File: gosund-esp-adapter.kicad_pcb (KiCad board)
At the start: 2 copper layers, 18.7 x 20.3 mm, 10 parts, among them J1 Connector, J2 Conn_01x04_Male, J3 Conn_01x01_Male, U1 ESP-M2

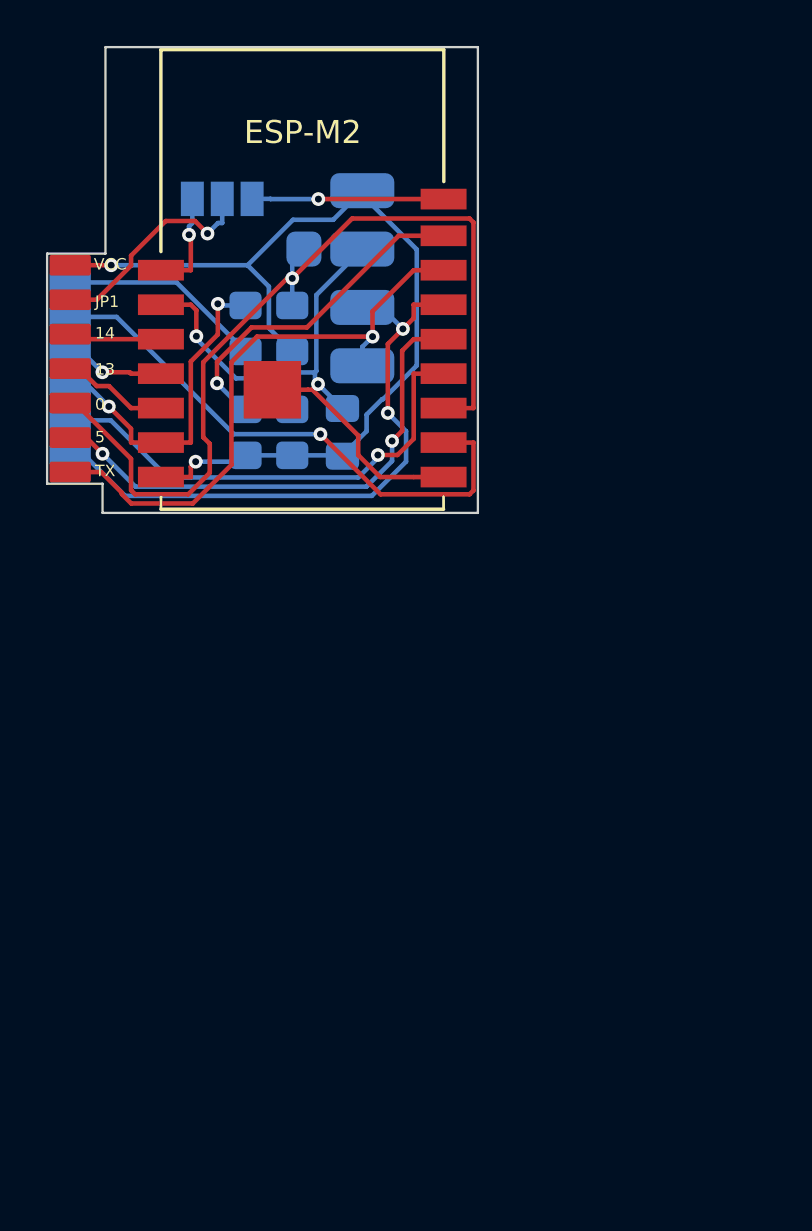
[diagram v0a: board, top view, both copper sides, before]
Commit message: modified to match the footprint of an ESP12f module
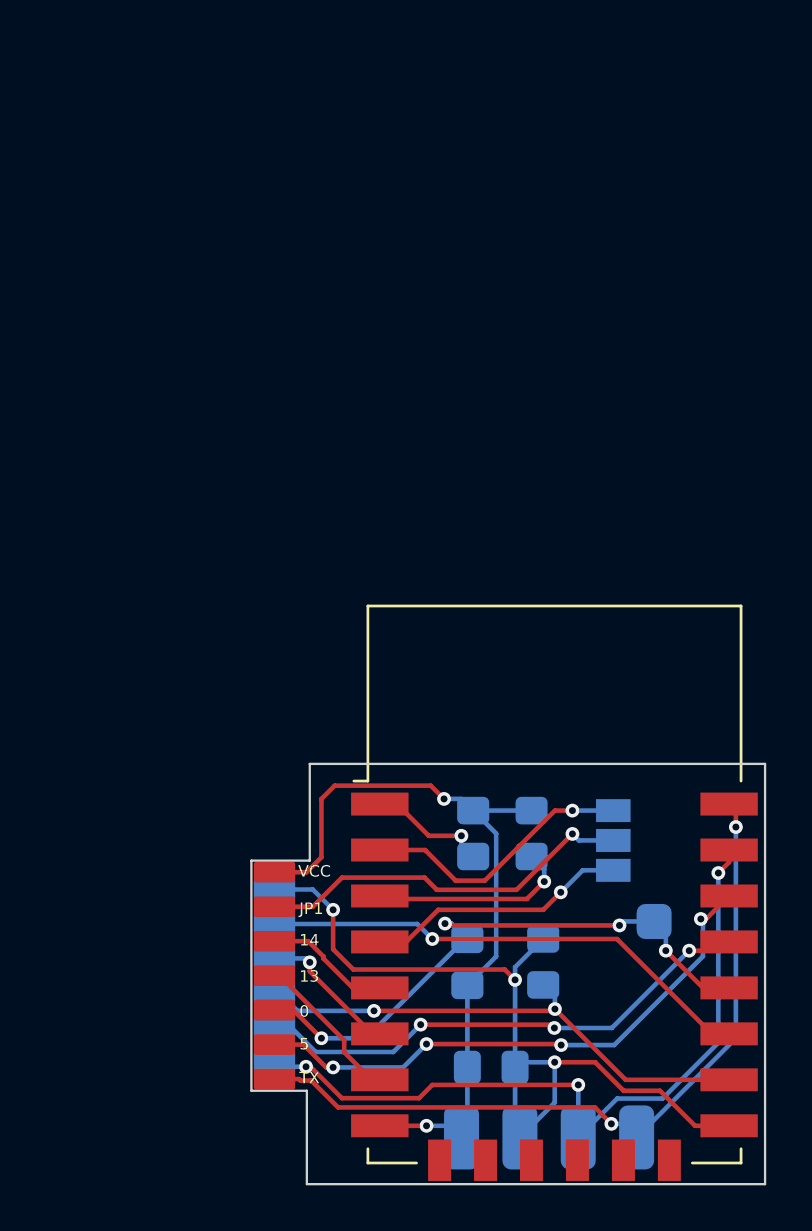
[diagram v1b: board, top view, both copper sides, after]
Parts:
- removed U1: ESP-M2, ESP8285:ESP-M2
- added G***: LOGO, ColossalTurtle:logo_smaller, B.Cu at (163.3, 119.4)
- added U2: ESP-12F, RF_Module:ESP-12E, F.Cu at (160.5, 112.9)
- moved J2 41.4 mm to (156.5, 124.0), turned to 90 degrees
- moved J3 33.0 mm to (162.3, 114.6)
- moved JP1 32.7 mm to (163.1, 111.0), turned to -90 degrees
- moved R4 30.5 mm to (160.0, 116.3), turned to 90 degrees
- moved R3 28.6 mm to (156.7, 116.3)
- moved C1 28.4 mm to (157.8, 120.9), turned to 0 degrees
- moved J1 27.9 mm to (149.2, 121.4)
- moved R1 20.3 mm to (159.5, 110.7), turned to -90 degrees
- moved R2 20.1 mm to (157.0, 110.7), turned to -90 degrees
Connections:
- R2 pad 2: /RST -> Net-(U2-~{RST})
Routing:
- net /RST: track 14.8 -> 0.00 mm, vias 1 -> 0
- net /IO0: track 40.3 -> 26.0 mm, vias 1 -> 4
- net /IO15: track 14.4 -> 22.7 mm
- net /ADC: track 4.50 -> 12.0 mm
- net /TX: track 25.8 -> 33.2 mm, vias 1 -> 2
- net VCC: track 41.0 -> 33.7 mm
- net /JP1: track 9.75 -> 16.6 mm
- net GND: track 30.4 -> 36.8 mm, vias 1 -> 3
- net /RX: track 27.1 -> 32.8 mm, vias 2 -> 3
- net Net-(U2-~{RST}): track 0.00 -> 5.24 mm, vias 0 -> 1
- net /IO16: track 8.34 -> 11.5 mm
- net /IO2: track 24.2 -> 21.8 mm
- net /IO13: track 4.66 -> 6.77 mm
- net /IO5: track 22.3 -> 24.4 mm, vias 2 -> 4
- net /IO12: track 4.35 -> 6.17 mm
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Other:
- board size 18.7 x 20.3 mm -> 22.4 x 18.3 mm
- board text added: "ESP-12F Adapter"
- board text added: "v1.0"
- board text removed: "(c) 2023 chrisklinger.de"
- board text removed: "ESP-M2 Adapter"
- board text removed: "Rev 3, 2023-04"
